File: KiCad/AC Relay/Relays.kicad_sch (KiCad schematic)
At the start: 14 parts, among them J2 Screw_Terminal_01x02, J3 Screw_Terminal_01x02, K1 1-2071556-1, K2 1-2071556-1, K3 1-2071556-1, K4 1-2071556-1, Q1 FDN537N, Q2 FDN537N, Q3 FDN537N, Q4 FDN537N

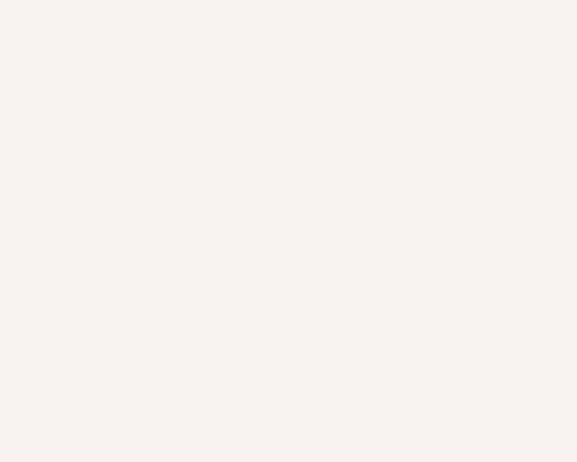
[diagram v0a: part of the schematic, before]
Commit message: error elemination
schametic error elemination
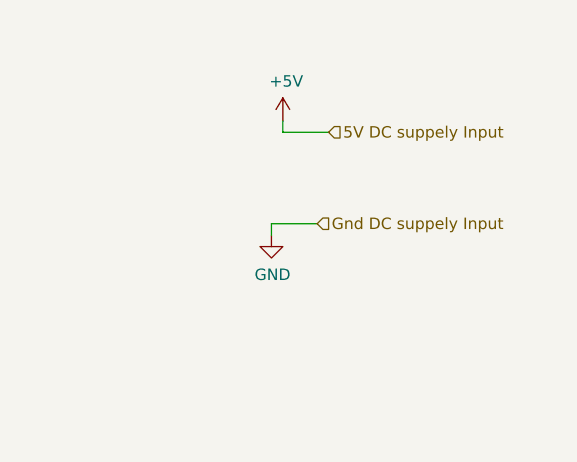
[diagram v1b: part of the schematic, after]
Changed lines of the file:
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@@
 	(wire
 		(pts
+			(xy 209.55 39.37) (xy 204.47 39.37)
+		)
+		(stroke
+			(width 0)
+			(type default)
+		)
+	)
+	(wire
+		(pts
 			(xy 34.29 60.96) (xy 41.91 60.96)
 		)
@@
 		)
 	)
+	(wire
+		(pts
+			(xy 204.47 39.37) (xy 204.47 40.64)
+		)
+		(stroke
+			(width 0)
+			(type default)
+		)
+	)
 	(polyline
 		(pts
@@
 	(wire
 		(pts
+			(xy 205.74 29.21) (xy 205.74 27.94)
+		)
+		(stroke
+			(width 0)
+			(type default)
+		)
+	)
+	(wire
+		(pts
 			(xy 50.8 104.14) (xy 63.5 104.14)
 		)
@@
 		)
 	)
+	(wire
+		(pts
+			(xy 205.74 29.21) (xy 210.82 29.21)
+		)
+		(stroke
+			(width 0)
+			(type default)
+		)
+	)
 	(polyline
 		(pts
@@
 		)
 	)
+	(hierarchical_label "Gnd DC suppely Input"
+		(shape input)
+		(at 209.55 39.37 0)
+		(fields_autoplaced yes)
+		(effects
+			(font
+				(size 1.27 1.27)
+			)
+			(justify left)
+		)
+	)
 	(hierarchical_label "Phase"
 		(shape input)
@@
 		)
 	)
+	(hierarchical_label "5V DC suppely Input"
+		(shape input)
+		(at 210.82 29.21 0)
+		(fields_autoplaced yes)
+		(effects
+			(font
+				(size 1.27 1.27)
+			)
+			(justify left)
+		)
+	)
 	(symbol
 		(lib_id "Connector:Screw_Terminal_01x02")
@@
 	)
 	(symbol
+		(lib_id "power:GND")
+		(at 204.47 40.64 0)
+		(unit 1)
+		(exclude_from_sim no)
+		(in_bom yes)
+		(on_board yes)
+		(dnp no)
+		(property "Reference" "#PWR041"
+			(at 204.47 46.99 0)
+			(effects
+				(font
+					(size 1.27 1.27)
+				)
+				(hide yes)
+			)
+		)
+		(property "Value" "GND"
+			(at 204.597 45.0342 0)
+			(effects
+				(font
+					(size 1.27 1.27)
+				)
+			)
+		)
+		(property "Footprint" ""
+			(at 204.47 40.64 0)
+			(effects
+				(font
+					(size 1.27 1.27)
+				)
+				(hide yes)
+			)
+		)
+		(property "Datasheet" ""
+			(at 204.47 40.64 0)
+			(effects
+				(font
+					(size 1.27 1.27)
+				)
+				(hide yes)
+			)
+		)
+		(property "Description" "Power symbol creates a global label with name \"GND\" , ground"
+			(at 204.47 40.64 0)
+			(effects
+				(font
+					(size 1.27 1.27)
+				)
+				(hide yes)
+			)
+		)
+		(pin "1"
+		)
+		(instances
+			(project "AC Relay"
+				(path "/fb13741d-37d5-4c22-9791-0e2ba86035f2/549a003a-5ad1-4e1d-a424-741fce4d057b"
+					(reference "#PWR041")
+					(unit 1)
+				)
+			)
+		)
+	)
+	(symbol
 		(lib_id "Device:Q_NMOS_GDSD")
 		(at 114.3 134.62 0)
@@
 					(unit 1)
 				)
+			)
+		)
+	)
+	(symbol
+		(lib_id "power:+5V")
+		(at 205.74 27.94 0)
+		(unit 1)
+		(exclude_from_sim no)
+		(in_bom yes)
+		(on_board yes)
+		(dnp no)
+		(property "Reference" "#PWR040"
+			(at 205.74 31.75 0)
+			(effects
+				(font
+					(size 1.27 1.27)
+				)
+				(hide yes)
+			)
+		)
+		(property "Value" "+5V"
+			(at 206.121 23.5458 0)
+			(effects
+				(font
+					(size 1.27 1.27)
+				)
+			)
+		)
+		(property "Footprint" ""
+			(at 205.74 27.94 0)
+			(effects
+				(font
+					(size 1.27 1.27)
+				)
+				(hide yes)
+			)
+		)
+		(property "Datasheet" ""
+			(at 205.74 27.94 0)
+			(effects
+				(font
+					(size 1.27 1.27)
+				)
+				(hide yes)
+			)
+		)
+		(property "Description" "Power symbol creates a global label with name \"+5V\""
+			(at 205.74 27.94 0)
+			(effects
+				(font
+					(size 1.27 1.27)
+				)
+				(hide yes)
+			)
+		)
+		(pin "1"
+		)
+		(instances
+			(project "AC Relay"
+				(path "/fb13741d-37d5-4c22-9791-0e2ba86035f2/549a003a-5ad1-4e1d-a424-741fce4d057b"
+					(reference "#PWR040")
+					(unit 1)
+				)
